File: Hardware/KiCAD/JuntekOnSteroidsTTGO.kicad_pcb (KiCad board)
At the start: 2 copper layers, 54.6 x 34.3 mm, 35 parts, among them J1 To PSU host board, J11 patch, J12 patch, J2 To PSU host board, J21 patch, J22 patch, J23 patch, J30 Expansion1, J4 ESP32-TFT, J5 ESP32-TFT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

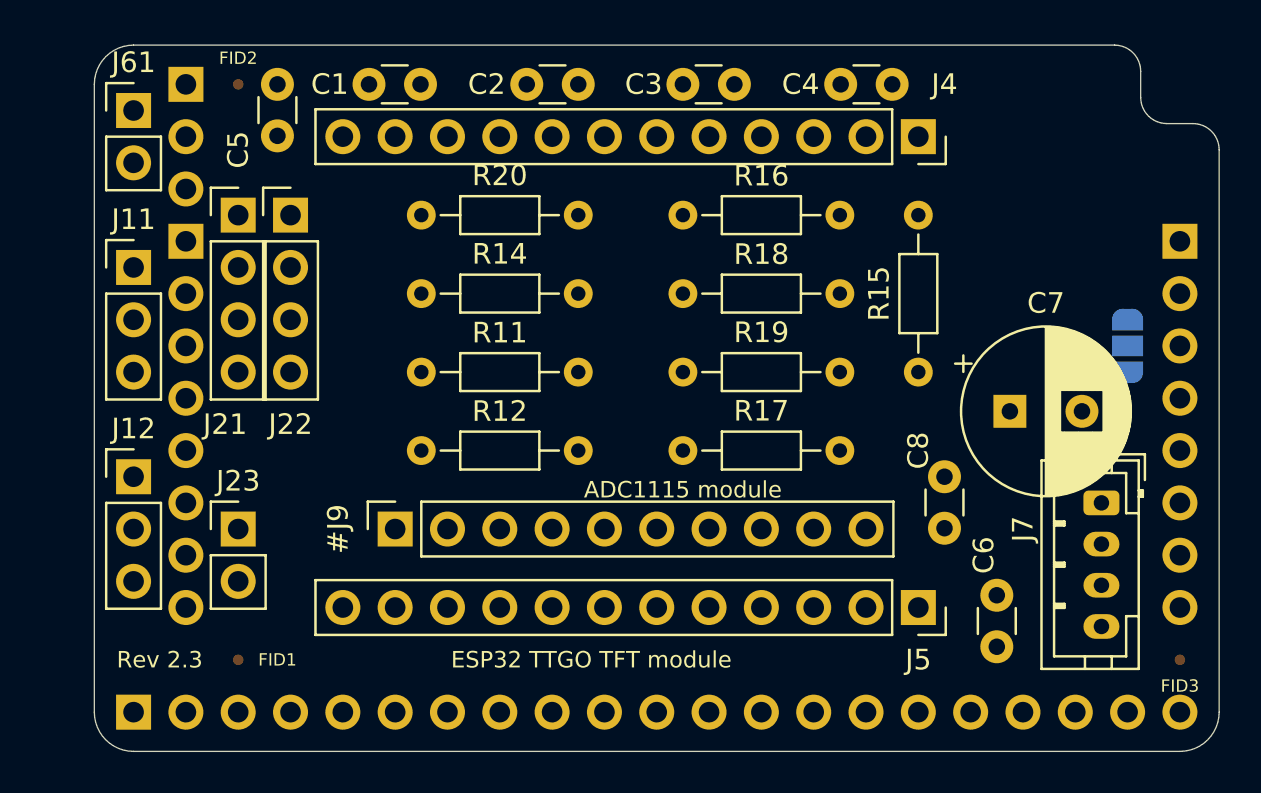
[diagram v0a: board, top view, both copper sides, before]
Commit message: 90-deg patch headers
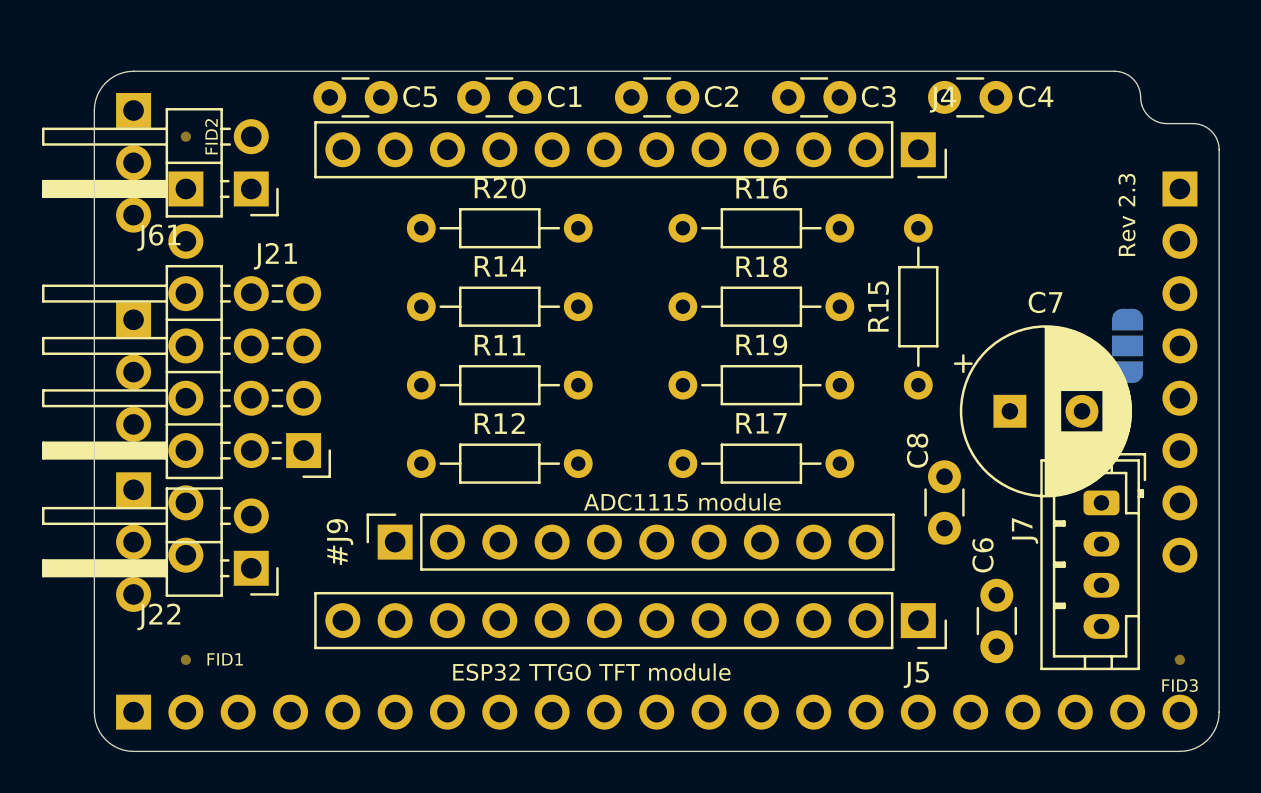
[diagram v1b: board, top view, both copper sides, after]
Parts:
- removed the J22 at (108.6, 66.7)
- J11, J12: footprint Connector_PinHeader_2.54mm:PinHeader_1x03_P2.54mm_Vertical -> Connector_PinHeader_2.54mm:PinHeader_1x03_P2.54mm_Horizontal; moved to B.Cu
- J21: footprint Connector_PinHeader_2.54mm:PinHeader_1x04_P2.54mm_Vertical -> Connector_PinHeader_2.54mm:PinHeader_2x04_P2.54mm_Horizontal
- J22: renamed from J23; footprint Connector_PinHeader_2.54mm:PinHeader_1x02_P2.54mm_Vertical -> Connector_PinHeader_2.54mm:PinHeader_1x02_P2.54mm_Horizontal
- J61: footprint Connector_PinHeader_2.54mm:PinHeader_1x02_P2.54mm_Vertical -> Connector_PinHeader_2.54mm:PinHeader_1x02_P2.54mm_Horizontal
- moved J21 11.9 mm to (109.2, 78.1), turned to 180 degrees
- moved J61 6.87 mm to (106.7, 65.4), turned to 180 degrees
- moved C3 5.16 mm to (132.8, 61.0)
- moved C1 5.12 mm to (117.5, 61.0)
- moved C2 5.12 mm to (127.6, 61.0)
- moved C4 5.08 mm to (142.8, 61.0)
- moved C5 5.08 mm to (113.0, 61.0), turned to 180 degrees
- moved FID2 3.59 mm to (103.5, 62.9)
- moved J6 2.84 mm to (101.0, 61.6)
- moved FID1 2.54 mm to (103.5, 88.3)
- moved J1 2.54 mm to (103.5, 65.4)
- moved J11 2.54 mm to (101.0, 71.8), turned to 180 degrees
- moved J2 2.54 mm to (151.8, 65.4)
- moved J22 2.01 mm to (106.7, 83.8), turned to 180 degrees
- moved J12 0.64 mm to (101.0, 80.0), turned to 180 degrees
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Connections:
- J21 pad 2: /A1 -> /ADC0
- J21 pad 3: /A2 -> /A1
- J21 pad 4: Net-(J21-Pad4) -> /ADC1
- J22 pad 1: /NotEnable -> /FanPWM
- J22 pad 2: /FanPWM -> /NotEnable
- J61 pad 1: /J6.2 -> /J6.3
- J61 pad 2: /J6.3 -> /J6.2
- R17 pad 1: Net-(J21-Pad4) -> Net-(J21-Pad7)
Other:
- board size 54.6 x 34.3 mm -> 54.6 x 33 mm

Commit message: routed
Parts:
- moved R18 21.7 mm to (114.9, 78.7), turned to 0 degrees
- moved R12 17.1 mm to (135.3, 67.3)
- moved R16 14.8 mm to (122.6, 74.9)
- moved R11 13.3 mm to (135.3, 71.1)
- moved R15 7.62 mm to (139.1, 74.9), turned to 90 degrees
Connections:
- J30 pad 1: Net-(J30-Pad1) -> /GND
- J30 pad 10: Net-(J30-Pad10) -> /GPIO26
- J30 pad 11: Net-(J30-Pad11) -> /GPIO27
- J30 pad 12: Net-(J30-Pad12) -> VCC
- J30 pad 2: Net-(J30-Pad2) -> /+3V3
- J30 pad 3: Net-(J30-Pad3) -> /SDA
- J30 pad 4: Net-(J30-Pad4) -> /SCL
- J30 pad 5: Net-(J30-Pad5) -> /GPIO17
- J30 pad 6: Net-(J30-Pad6) -> /GPIO13
- J30 pad 7: Net-(J30-Pad7) -> /GPIO2
- J30 pad 8: Net-(J30-Pad8) -> /GPIO12
- J30 pad 9: Net-(J30-Pad9) -> /GPIO25
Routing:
- net /GND: track 0.00 -> 186.9 mm
- net VCC: track 0.00 -> 98.8 mm, vias 0 -> 2
- net /+3V3: track 0.00 -> 93.8 mm
- net /GPIO12: track 0.00 -> 74.4 mm
- net /SCL: track 0.00 -> 50.0 mm
- net /SDA: track 0.00 -> 48.8 mm
- net /GPIO17: track 0.00 -> 47.0 mm
- net /ADC3: track 0.00 -> 46.9 mm
- net /GPIO13: track 0.00 -> 46.4 mm
- net /GPIO27: track 0.00 -> 38.4 mm
- net /GPIO25: track 0.00 -> 37.8 mm
- net /GPIO26: track 0.00 -> 37.8 mm
- net /NotEnable: track 0.00 -> 37.1 mm
- net /ADC2: track 0.00 -> 35.9 mm
- net /ADC1: track 0.00 -> 34.7 mm
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- added copper zone on B.Cu, net /GND
- added copper zone on F.Cu, net /GND
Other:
- net class Default: clearance 0.2 -> 0.13; trace_width 0.25 -> 0.22
- net class thick added: clearance 0.13, trace_width 0.57, via_dia 0.8, via_drill 0.4
- rule trace_clearance: 0.2 -> 0.13
- rule trace_min: 0.2 -> 0.1
- board text added: "12/34"
- board text added: "I2C"
- board text added: "Rev 2.4"
- board text removed: "12 34"
- board text removed: "Rev 2.3"

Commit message: AltVinSense replacing LoadPWM
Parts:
- removed R19: 10k/none, Resistor_THT:R_Axial_DIN0204_L3.6mm_D1.6mm_P7.62mm_Horizontal
- added R13: 1k/zero, Resistor_THT:R_Axial_DIN0204_L3.6mm_D1.6mm_P7.62mm_Horizontal, F.Cu at (127.6, 74.9)
- J61: footprint Connector_PinHeader_2.54mm:PinHeader_1x02_P2.54mm_Horizontal -> Connector_PinHeader_2.54mm:PinHeader_1x03_P2.54mm_Horizontal
- moved C4 3.14 mm to (139.7, 61.0)
- moved C3 2.58 mm to (130.2, 61.0)
- moved J21 2.54 mm to (109.2, 80.6)
- moved J61 2.54 mm to (106.7, 67.9)
- moved C2 1.95 mm to (125.7, 61.0)
- moved J22 1.91 mm to (106.7, 85.7)
- moved C1 1.27 mm to (116.2, 61.0)
- moved C5 1.23 mm to (111.8, 61.0)
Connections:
- J21 pad 5: /A2 -> Net-(J21-Pad5)
- J6 pad 1: /GPIO12 -> /J6.1
- R20 pad 1: /ADC0 -> /J6.1
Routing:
- net /GPIO12: track 74.4 -> 14.5 mm
- net Net-(J21-Pad5): track 0.00 -> 19.4 mm
- net /J6.1: track 0.00 -> 16.3 mm
- net /A2: track 29.2 -> 15.1 mm
- net /GND: track 186.9 -> 176.8 mm
- net /ADC0: track 29.4 -> 32.1 mm
- net /NotEnable: track 37.1 -> 39.7 mm
- net /ADC3: track 46.9 -> 44.4 mm
- net Net-(J21-Pad7): track 21.8 -> 24.1 mm
- net /A0: track 24.9 -> 22.8 mm
- net /A1: track 26.7 -> 24.6 mm
- net /ADC2: track 35.9 -> 34.4 mm
- net /J6.3: track 7.65 -> 6.24 mm
- net /ADC1: track 34.7 -> 33.8 mm
- net /FanPWM: track 10.4 -> 11.1 mm
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
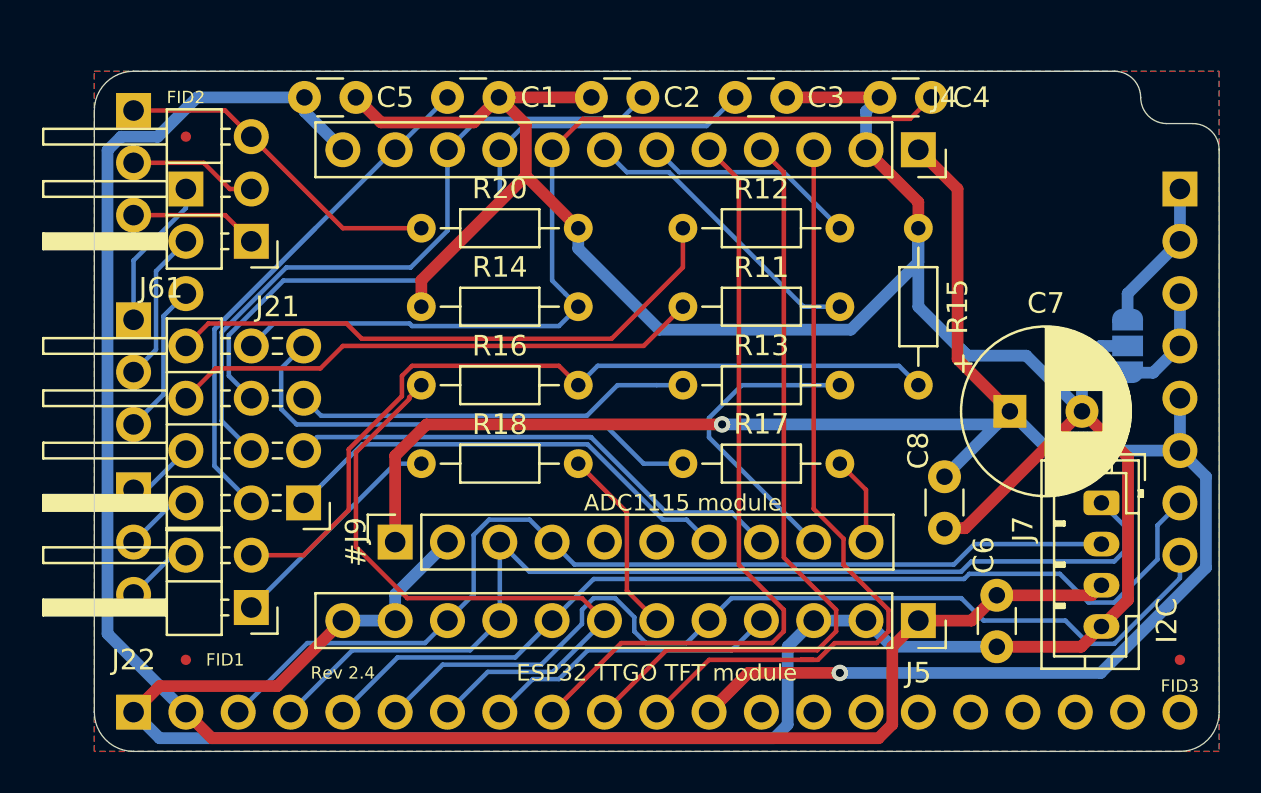
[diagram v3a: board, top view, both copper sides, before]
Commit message: Change ADS115 to 3.3V & other tweaks
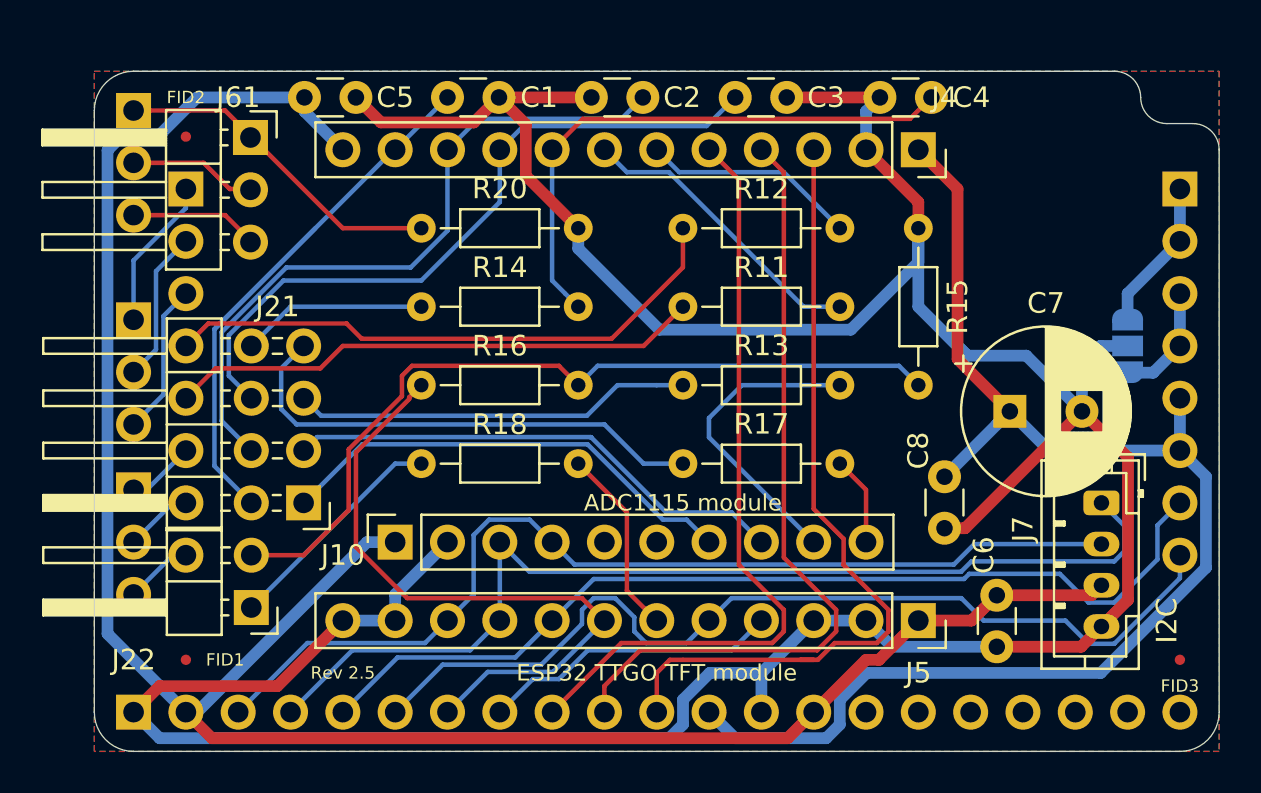
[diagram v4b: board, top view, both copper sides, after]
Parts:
- removed #J9: ADS1115, Connector_PinSocket_2.54mm:PinSocket_1x10_P2.54mm_Vertical
- added J10: ADS1115, Connector_PinSocket_2.54mm:PinSocket_1x10_P2.54mm_Vertical, F.Cu at (113.7, 82.5)
- R14: value 1k/none -> 1k/zero
- moved R14 7.62 mm to (122.6, 71.1), turned to 180 degrees
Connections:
- net /NotEnable renamed Net-(J22-Pad2)
- J21 pad 8: /ADC3 -> Net-(J21-Pad8)
- J22 pad 1: /FanPWM -> Net-(J22-Pad1)
- J30 pad 13: Net-(J30-Pad13) -> /GND
- J30 pad 14: Net-(J30-Pad14) -> /+3V3
- J5 pad 6: /GPIO15 -> /FanPWM
- J61 pad 1: /J6.3 -> /J6.1
- J61 pad 3: /J6.1 -> /J6.3
- R14 pad 1: /GND -> /ADC3
- R14 pad 2: /ADC3 -> Net-(J21-Pad8)
- R18 pad 1: /FanPWM -> Net-(J22-Pad1)
- R18 pad 2: /GPIO15 -> /FanPWM
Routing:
- net VCC: track 98.8 -> 66.5 mm, vias 2 -> 0
- net /ADC3: track 44.4 -> 27.6 mm
- net /+3V3: track 93.1 -> 104.4 mm
- net Net-(J22-Pad1): track 0.00 -> 11.1 mm
- net /GPIO15: track 9.20 -> 0.00 mm
- net Net-(J21-Pad8): track 0.00 -> 9.04 mm
- net /GND: track 176.8 -> 168.8 mm
- net /FanPWM: track 11.1 -> 9.20 mm
- net /GPIO27: track 38.4 -> 39.5 mm
- net /GPIO26: track 37.8 -> 38.5 mm
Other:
- board text added: "Rev 2.5"
- board text removed: "All 4 traces to all 4 pins to enable choice of I2C pinout standard. E.g. DFRobot vs [Grove, Crowtail, QWIIC, nodeLynk, STEMMA(QT)] Not inc. Quick2Wire & BreakoutGarden"
- board text removed: "Rev 2.4"
